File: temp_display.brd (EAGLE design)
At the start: 101.6 x 76.2 mm, 62 parts, among them IC2 ATMEGA168PROUND, Q1 2N2907, T1 BC547

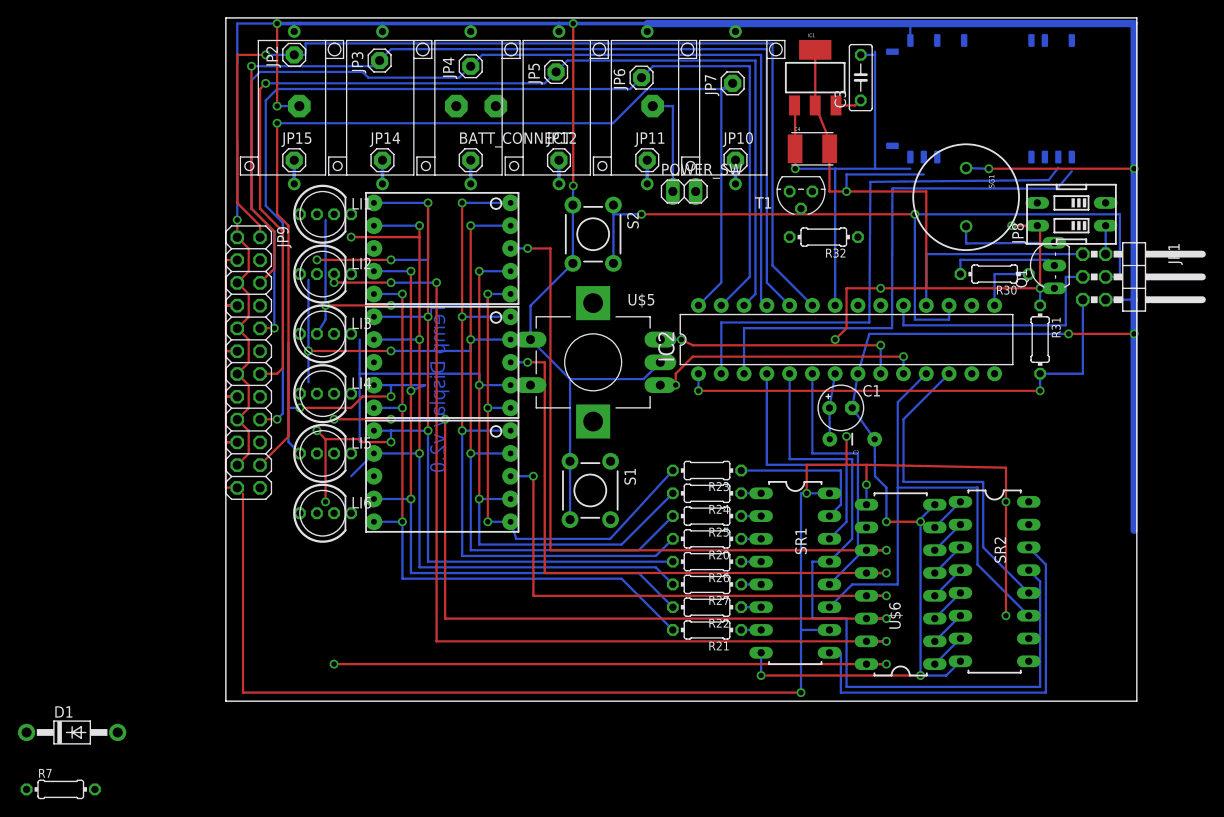
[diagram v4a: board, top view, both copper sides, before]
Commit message: Last version with CR2032 batteries
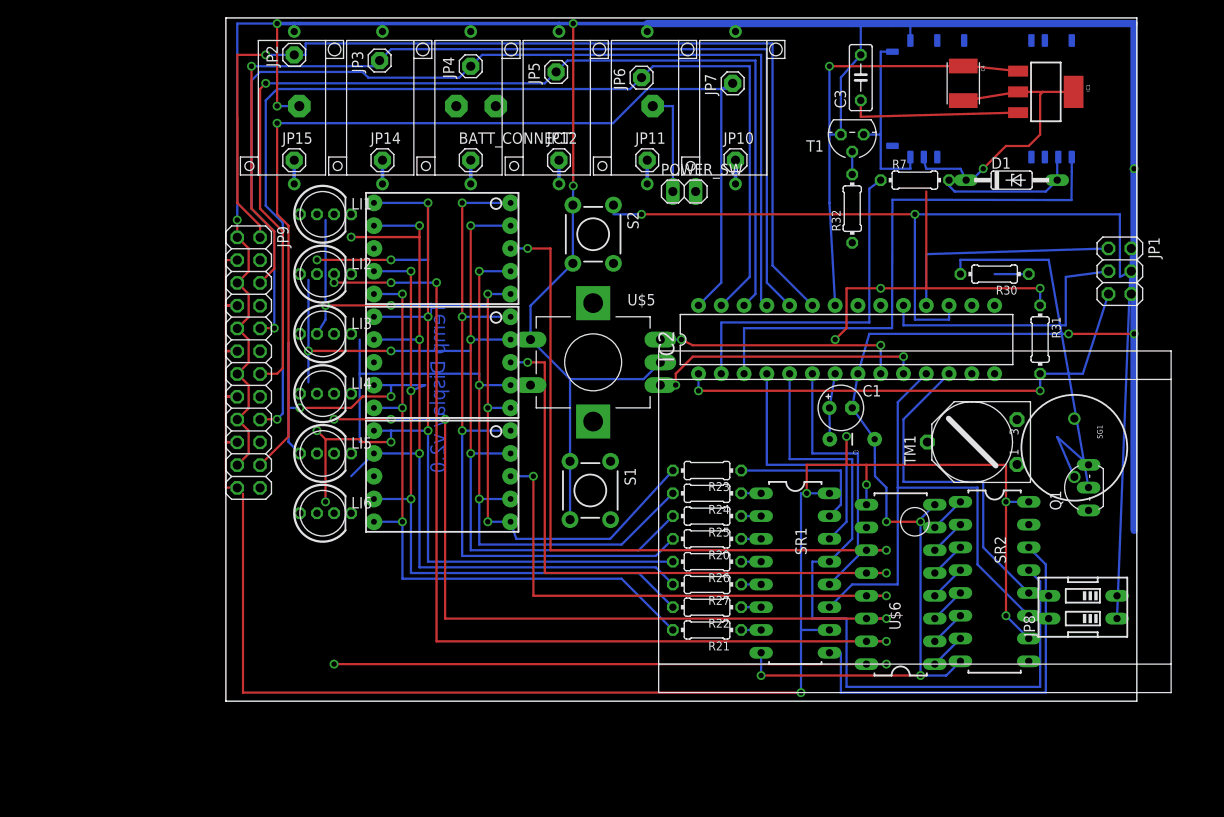
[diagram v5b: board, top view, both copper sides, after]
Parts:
- added TM1: (no value), kirill:TRIMPOT_A
- added U$2: BATTERY3XAAA, kirill:BATTERY_HOLDER_3XAAA
- D1: value 1N4004 -> 1N821; device adafruit:DO41-10 -> diode:DO35Z10
- JP1: device pinhead:2X03/90 -> pinhead:2X03
- moved D1 121.5 mm to (87.6, 57.8)
- moved R7 117.0 mm to (76.8, 57.8)
- moved JP8 43.8 mm to (95.6, 10.2)
- moved SG1 30.4 mm to (94.6, 27.9)
- moved IC1 25.8 mm to (91.4, 67.6), turned to 270 degrees
- moved Q1 25.1 mm to (94.9, 23.5)
- moved C4 18.3 mm to (82.2, 68.6), turned to 270 degrees
- moved T1 8.54 mm to (69.8, 62.9)
- moved R32 4.49 mm to (69.8, 54.6), turned to 90 degrees
- moved JP1 2.31 mm to (99.7, 47.6)
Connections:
- removed net N$48: IC2.15, R30.1
- new net N$5: IC2.16, S2.1, S2.2
- new net N$6: SG1.-, TM1.E
- net GND: now also TM1.S; no longer SG1.-
- net N$34: now also R30.1; no longer S2.1, S2.2
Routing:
- net N$30: track 3.17 -> 41.3 mm
- net VCC: track 76.8 -> 40.5 mm, vias 5 -> 3
- net N$51: track 12.3 -> 37.2 mm
- net +3V3: track 11.3 -> 34.2 mm, vias 0 -> 1
- net +5V: track 211.0 -> 233.8 mm
- net N$3: track 0.00 -> 20.9 mm
- net SERIAL_RX: track 59.5 -> 38.7 mm
- net N$4: track 0.00 -> 16.1 mm
- net GND: track 475.5 -> 467.3 mm, vias 14 -> 13
- net N$48: track 7.30 -> 0.00 mm
- net N$43: track 27.6 -> 30.5 mm
- net N$27: track 23.2 -> 26.0 mm
- net N$34: track 88.7 -> 85.8 mm
- net SERIAL_TX: track 58.1 -> 60.7 mm
- net N$2: track 0.00 -> 2.54 mm
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
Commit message: 
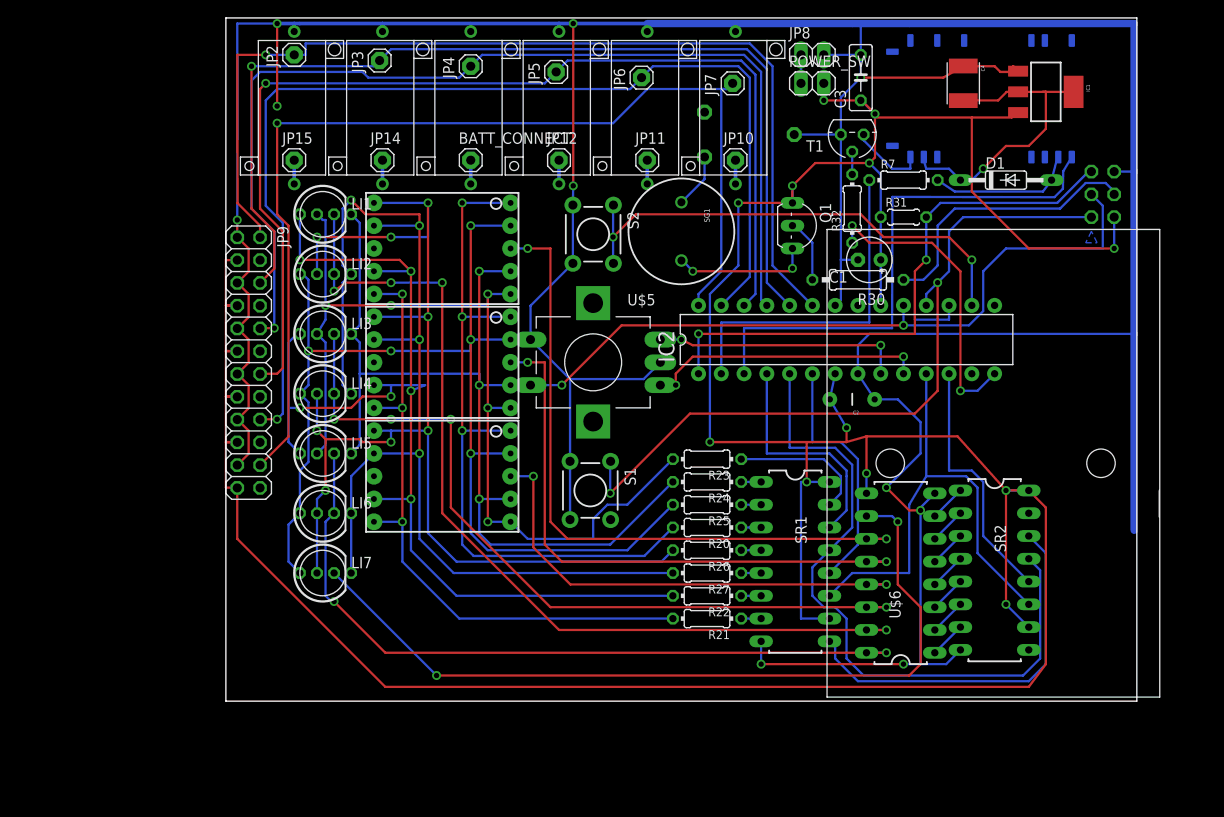
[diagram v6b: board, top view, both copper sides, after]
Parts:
- removed BAT1, BAT2: (no value), kirill:BATT_CR2032H_EBAY1
- added LI7: (no value), kirill:LED_RGB_5MM_
- JP8: device SparkFun:DIPSWITCH-02 -> pinhead:1X02
- R30: device resistor:0204/7 -> resistor:0207/10
- R31: device resistor:0204/7 -> resistor:0204/5
- R7: value (none) -> 1K
- moved JP8 68.6 mm to (65.4, 71.8), turned to 0 degrees
- moved SG1 50.0 mm to (50.8, 52.1)
- moved TM1 45.5 mm to (55.9, 62.9), flipped to the bottom
- moved Q1 42.2 mm to (64.5, 52.7), turned to 270 degrees
- moved R31 20.5 mm to (75.6, 53.7), turned to 0 degrees
- moved POWER_SW 18.7 mm to (65.4, 68.6)
- moved C1 16.8 mm to (71.8, 48.9), turned to 180 degrees
- moved R30 15.3 mm to (70.5, 46.7)
- moved U$2 12.6 mm to (85.1, 29.2), turned to 180 degrees
- moved JP1 8.78 mm to (97.8, 56.2), flipped to the bottom, turned to 90 degrees
- moved C2 4.45 mm to (69.8, 33.3)
- moved R23 1.27 mm to (53.7, 26.7)
- moved R26 1.27 mm to (53.7, 16.5)
- moved R27 1.27 mm to (53.7, 14.0)
- moved U$6 1.27 mm to (75.2, 14.0)
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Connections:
- net K_IL56 renamed K_IL567
- net N$43 renamed MROUTE
- net N$50 renamed CAT_1
- net N$53 renamed CAT_2
- net N$54 renamed CAT_3
- net N$55 renamed CAT_4
- net N$56 renamed CAT_5
- net N$57 renamed CAT_6
- net N$58 renamed CAT_7
- removed net B1: BAT2.-, POWER_SW.1
- removed net BATT_CONNECT: BAT1.-, BAT2.+
- removed net N$30: JP1.2, JP8.1
- removed net VCC: R31.1
- new net +5: C1.+, C2.2, C3.1, IC1.3, IC2.20, IC2.7, JP1.2, JP9.11, JP9.15, JP9.19, JP9.23, JP9.3, JP9.7, POWER_SW.2, Q1.E, R31.1, SR1.10, SR1.16, SR2.10, SR2.16, U$6.9
- new net GND1: U$1.21
- new net GND2: U$1.22
- new net N$7: LI7.K, U$6.10
- new net N$9: SR2.15
- net +5V: now also JP8.1, POWER_SW.1; no longer C1.+, C2.2, C3.1, IC1.3, IC2.20, IC2.7, JP8.4, JP9.11, JP9.15, JP9.19, JP9.23, JP9.3, JP9.7, POWER_SW.2, Q1.E, SR1.10, SR1.16, SR2.10, SR2.16, U$6.9
- net GND: now also JP8.2; no longer BAT1.+, U$1.22
- net N$3: no longer U$1.21
- net N$6: now also TM1.A; no longer TM1.E
- net SEG_A: now also LI7.A_R
- net SEG_B: now also LI7.A_G
- net SEG_C: now also LI7.A_B
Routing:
- net +5: track 0.00 -> 386.5 mm, vias 0 -> 12
- net +5V: track 233.8 -> 3.17 mm, vias 6 -> 0
- net N$7: track 0.00 -> 91.3 mm, vias 0 -> 2
- net N$27: track 26.0 -> 82.8 mm, vias 0 -> 2
- net N$5: track 0.00 -> 54.8 mm, vias 0 -> 2
- net MROUTE: track 30.5 -> 81.5 mm, vias 0 -> 2
- net N$34: track 85.8 -> 41.1 mm, vias 2 -> 0
- net N$30: track 41.3 -> 0.00 mm
- net VCC: track 40.5 -> 0.00 mm, vias 3 -> 0
- net BTH_PW_TRANS: track 0.00 -> 34.0 mm, vias 0 -> 2
- net SEG_A: track 93.6 -> 127.1 mm
- net N$51: track 37.2 -> 7.14 mm
- net SEG_C: track 104.4 -> 128.6 mm
- net K_IL567: track 63.8 -> 83.7 mm
- net SEG_F: track 105.8 -> 123.9 mm, vias 5 -> 6
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- added copper zone on layer 16, net N$8
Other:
- board text removed: "Temp Display v2.0"

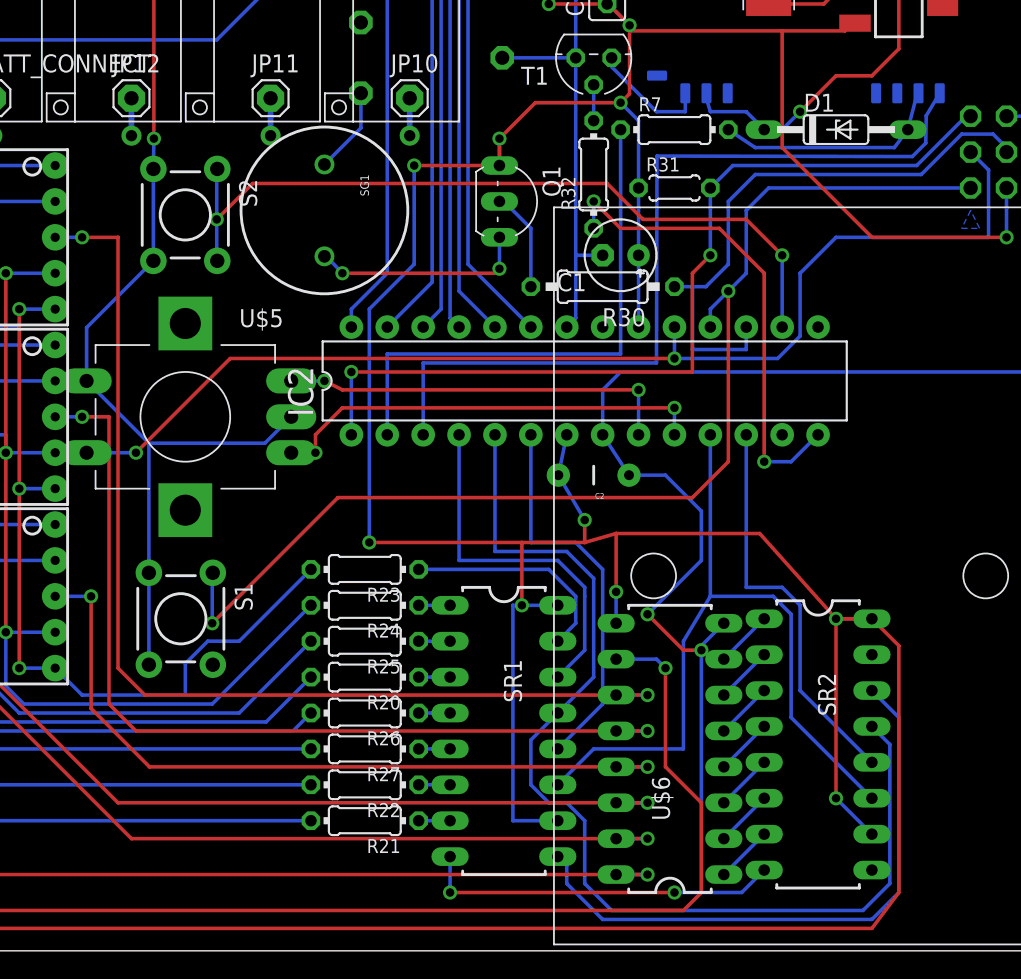
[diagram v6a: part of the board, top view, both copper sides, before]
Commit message: Reworked the schematic to allow adding an external oscillator. Still need to build this on the proto board.
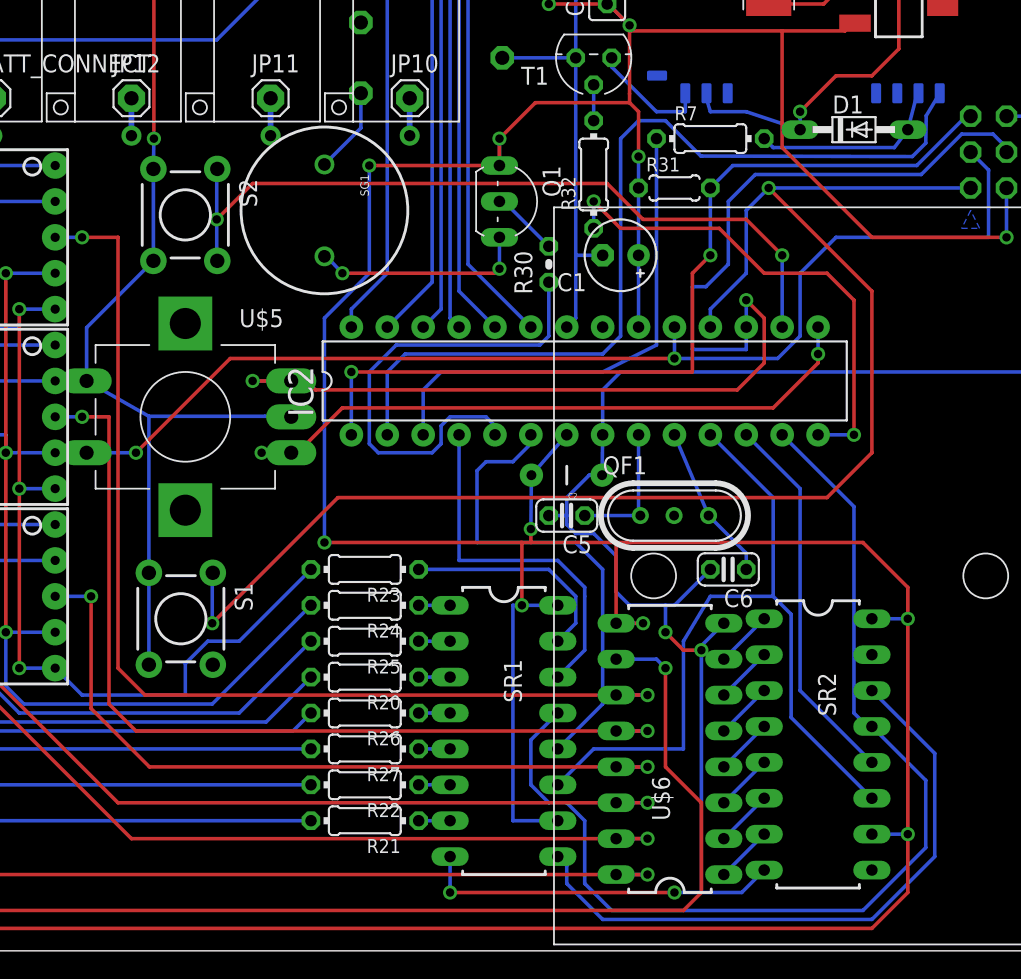
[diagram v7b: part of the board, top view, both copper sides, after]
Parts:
- added C5, C6: (no value), resistor:C025-024X044
- added QF1: 8M10AHC49T, crystal:HC49U
- D1: value 1N821 -> BAS15; device diode:DO35Z10 -> diode:DO34-7
- R30: device resistor:0207/10 -> resistor:0204V
- R32: value (none) -> 1K
- R7: value 1K -> 10K
- moved R30 4.13 mm to (66.7, 48.3), turned to 90 degrees
- moved R7 2.62 mm to (78.1, 57.1)
- moved C2 1.91 mm to (67.9, 33.3)
- moved D1 1.27 mm to (88.3, 57.8)
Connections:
- removed net N$34: IC2.17, JP1.4, R30.1
- new net N$10: IC2.5, R30.1
- new net N$11: C5.1, IC2.9, QF1.1
- new net N$12: C6.1, IC2.10, QF1.3
- net GND: now also C5.2, C6.2
- net N$31: now also IC2.17, JP1.4; no longer IC2.9
- net N$41: now also IC2.15; no longer IC2.10
- net OE: now also IC2.13; no longer IC2.5
- net SERIAL_RX: now also IC2.3; no longer IC2.2
- net SERIAL_TX: now also IC2.2; no longer IC2.3
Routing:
- net N$31: track 27.9 -> 86.7 mm
- net N$34: track 41.1 -> 0.00 mm
- net N$10: track 0.00 -> 34.5 mm
- net N$27: track 82.8 -> 102.9 mm
- net N$41: track 31.1 -> 46.6 mm
- net N$12: track 0.00 -> 11.1 mm
- net N$11: track 0.00 -> 9.70 mm
- net STCP1: track 27.5 -> 34.0 mm
- net GND: track 467.1 -> 473.0 mm
- net SERIAL_TX: track 59.4 -> 63.3 mm
- net SERIAL_RX: track 38.1 -> 35.3 mm
- net N$4: track 16.4 -> 13.8 mm
- net N$51: track 7.14 -> 4.81 mm
- net N$1: track 42.6 -> 44.7 mm
- net SHCP: track 54.3 -> 56.2 mm
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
